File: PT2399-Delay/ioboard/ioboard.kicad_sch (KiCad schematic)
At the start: 12 parts, among them J2 Conn_02x05_Odd_Even

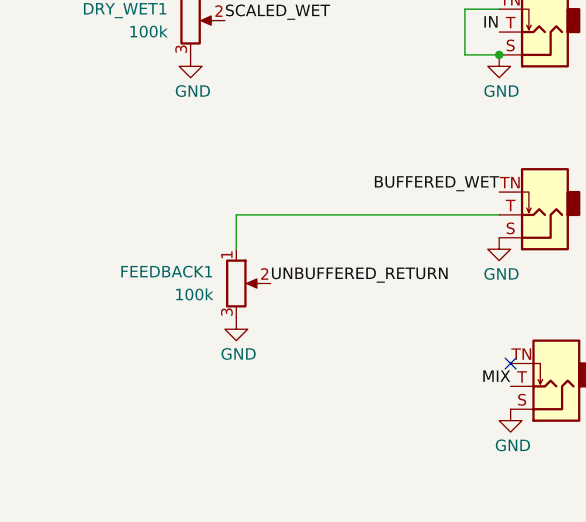
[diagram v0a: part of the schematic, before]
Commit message: Fixed feedback orientation (pin 1 should point low)
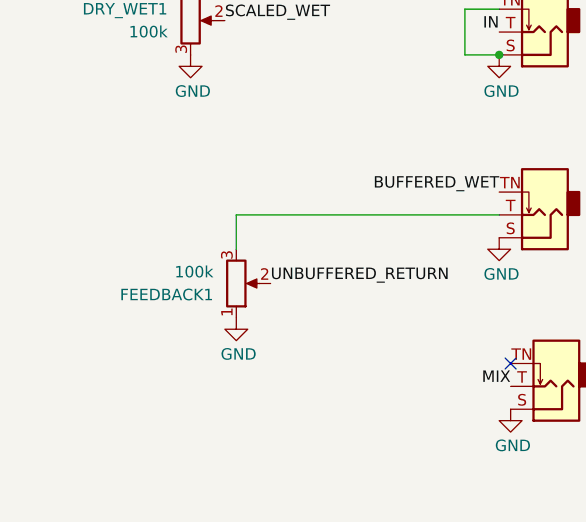
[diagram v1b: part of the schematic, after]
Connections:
- net GND: now also FEEDBACK1.1; no longer FEEDBACK1.3
- net at RETURN1.T: now also FEEDBACK1.3; no longer FEEDBACK1.1
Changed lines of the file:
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@@
 		(lib_id "Device:R_Potentiometer")
 		(at 91.44 93.98 0)
+		(mirror x)
 		(unit 1)
 		(exclude_from_sim no)
@@
 		(on_board yes)
 		(dnp no)
-		(fields_autoplaced yes)
 		(property "Reference" "FEEDBACK1"
-			(at 88.9 92.7099 0)
+			(at 88.9 95.2501 0)
 			(effects
 				(font
@@
 		)
 		(property "Value" "100k"
-			(at 88.9 95.2499 0)
+			(at 88.9 92.7101 0)
 			(effects
 				(font

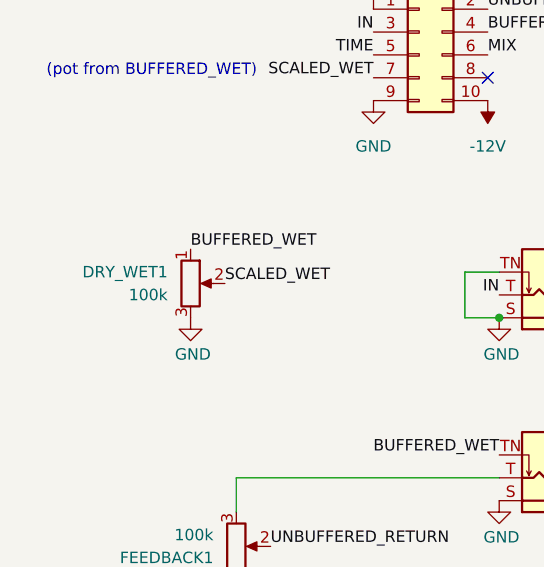
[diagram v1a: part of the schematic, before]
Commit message: Fixed up pinout of dry/wet as well
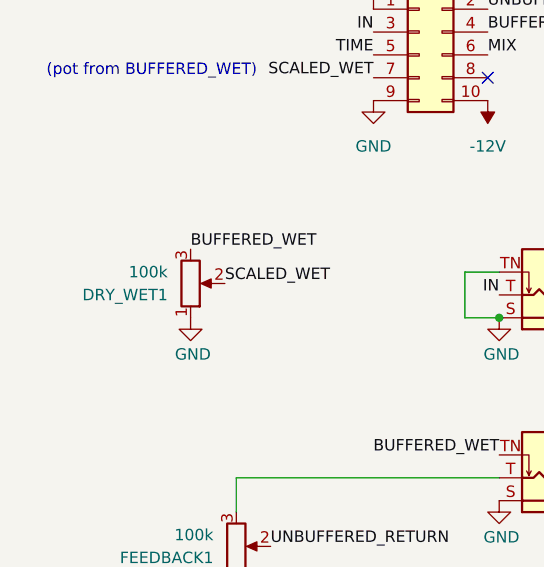
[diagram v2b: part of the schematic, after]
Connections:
- net BUFFERED_WET: now also DRY_WET1.3; no longer DRY_WET1.1
- net GND: now also DRY_WET1.1; no longer DRY_WET1.3
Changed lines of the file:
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@@
 		(lib_id "Device:R_Potentiometer")
 		(at 86.36 64.77 0)
+		(mirror x)
 		(unit 1)
 		(exclude_from_sim no)
@@
 		(on_board yes)
 		(dnp no)
-		(fields_autoplaced yes)
 		(property "Reference" "DRY_WET1"
-			(at 83.82 63.4999 0)
+			(at 83.82 66.0401 0)
 			(effects
 				(font
@@
 		)
 		(property "Value" "100k"
-			(at 83.82 66.0399 0)
+			(at 83.82 63.5001 0)
 			(effects
 				(font
